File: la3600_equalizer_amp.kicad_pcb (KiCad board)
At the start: 2 copper layers, 54 parts, among them J1 JACK_TRS_3PINS, J2 JACK_TRS_3PINS, J3 USB_B, U1 LA3600, U2 LA3600, U3 LM386, U4 LM386

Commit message: some more pcb layout work
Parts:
- moved C32 4.00 mm to (176.7, 66.9), turned to 90 degrees
- moved C33 3.65 mm to (176.5, 94.6), turned to 90 degrees
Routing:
- net Vcc: track 11.9 -> 205.0 mm, vias 0 -> 2
- net Net-(22K6-Pad4): track 0.00 -> 133.1 mm, vias 0 -> 2
- net Net-(22K1-Pad1): track 145.5 -> 226.1 mm, vias 8 -> 10
- net Net-(22K6-Pad1): track 0.00 -> 74.1 mm
- net Net-(22K1-Pad3): track 170.1 -> 236.0 mm, vias 0 -> 2
- net Net-(22K1-Pad4): track 161.6 -> 225.8 mm, vias 8 -> 10
- net Net-(C24-Pad1): track 0.00 -> 21.4 mm
- net Net-(C26-Pad1): track 0.00 -> 17.4 mm
- net Net-(C5-Pad1): track 0.00 -> 11.5 mm
- net Net-(C11-Pad2): track 0.00 -> 11.5 mm
- net Net-(C10-Pad2): track 0.00 -> 11.5 mm
- net Net-(C4-Pad1): track 0.00 -> 11.2 mm
- net Net-(C32-Pad1): track 0.00 -> 7.84 mm
- net Net-(C33-Pad1): track 0.00 -> 7.64 mm
- net Net-(C21-Pad1): track 0.00 -> 7.14 mm
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
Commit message: finish pcb layout
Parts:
- moved C35 8.92 mm to (202.2, 91.5), turned to 270 degrees
- moved C36 8.03 mm to (212.7, 68.6)
- moved C37 8.03 mm to (212.7, 80.6)
- moved J2 8.03 mm to (228.4, 74.4)
- moved C34 7.03 mm to (197.6, 63.5), turned to 270 degrees
- moved R4 3.18 mm to (198.1, 94.0), turned to 90 degrees
- moved R3 0.25 mm to (194.1, 66.0), turned to 90 degrees
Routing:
- net GND: track 0.00 -> 658.9 mm, vias 0 -> 12
- net Net-(22K6-Pad5): track 0.00 -> 71.8 mm, vias 0 -> 2
- net Net-(22K6-Pad2): track 0.00 -> 48.1 mm, vias 0 -> 2
- net Net-(C37-Pad1): track 0.00 -> 42.6 mm
- net Net-(C36-Pad2): track 0.00 -> 26.2 mm
- net Net-(C36-Pad1): track 0.00 -> 25.6 mm
- net Net-(C37-Pad2): track 0.00 -> 14.2 mm
- net Net-(J3-Pad5): track 0.00 -> 13.5 mm
- net Net-(C35-Pad1): track 0.00 -> 9.34 mm
- net Net-(C34-Pad1): track 0.00 -> 9.09 mm
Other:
- board outline added: 198.6 x 95 mm

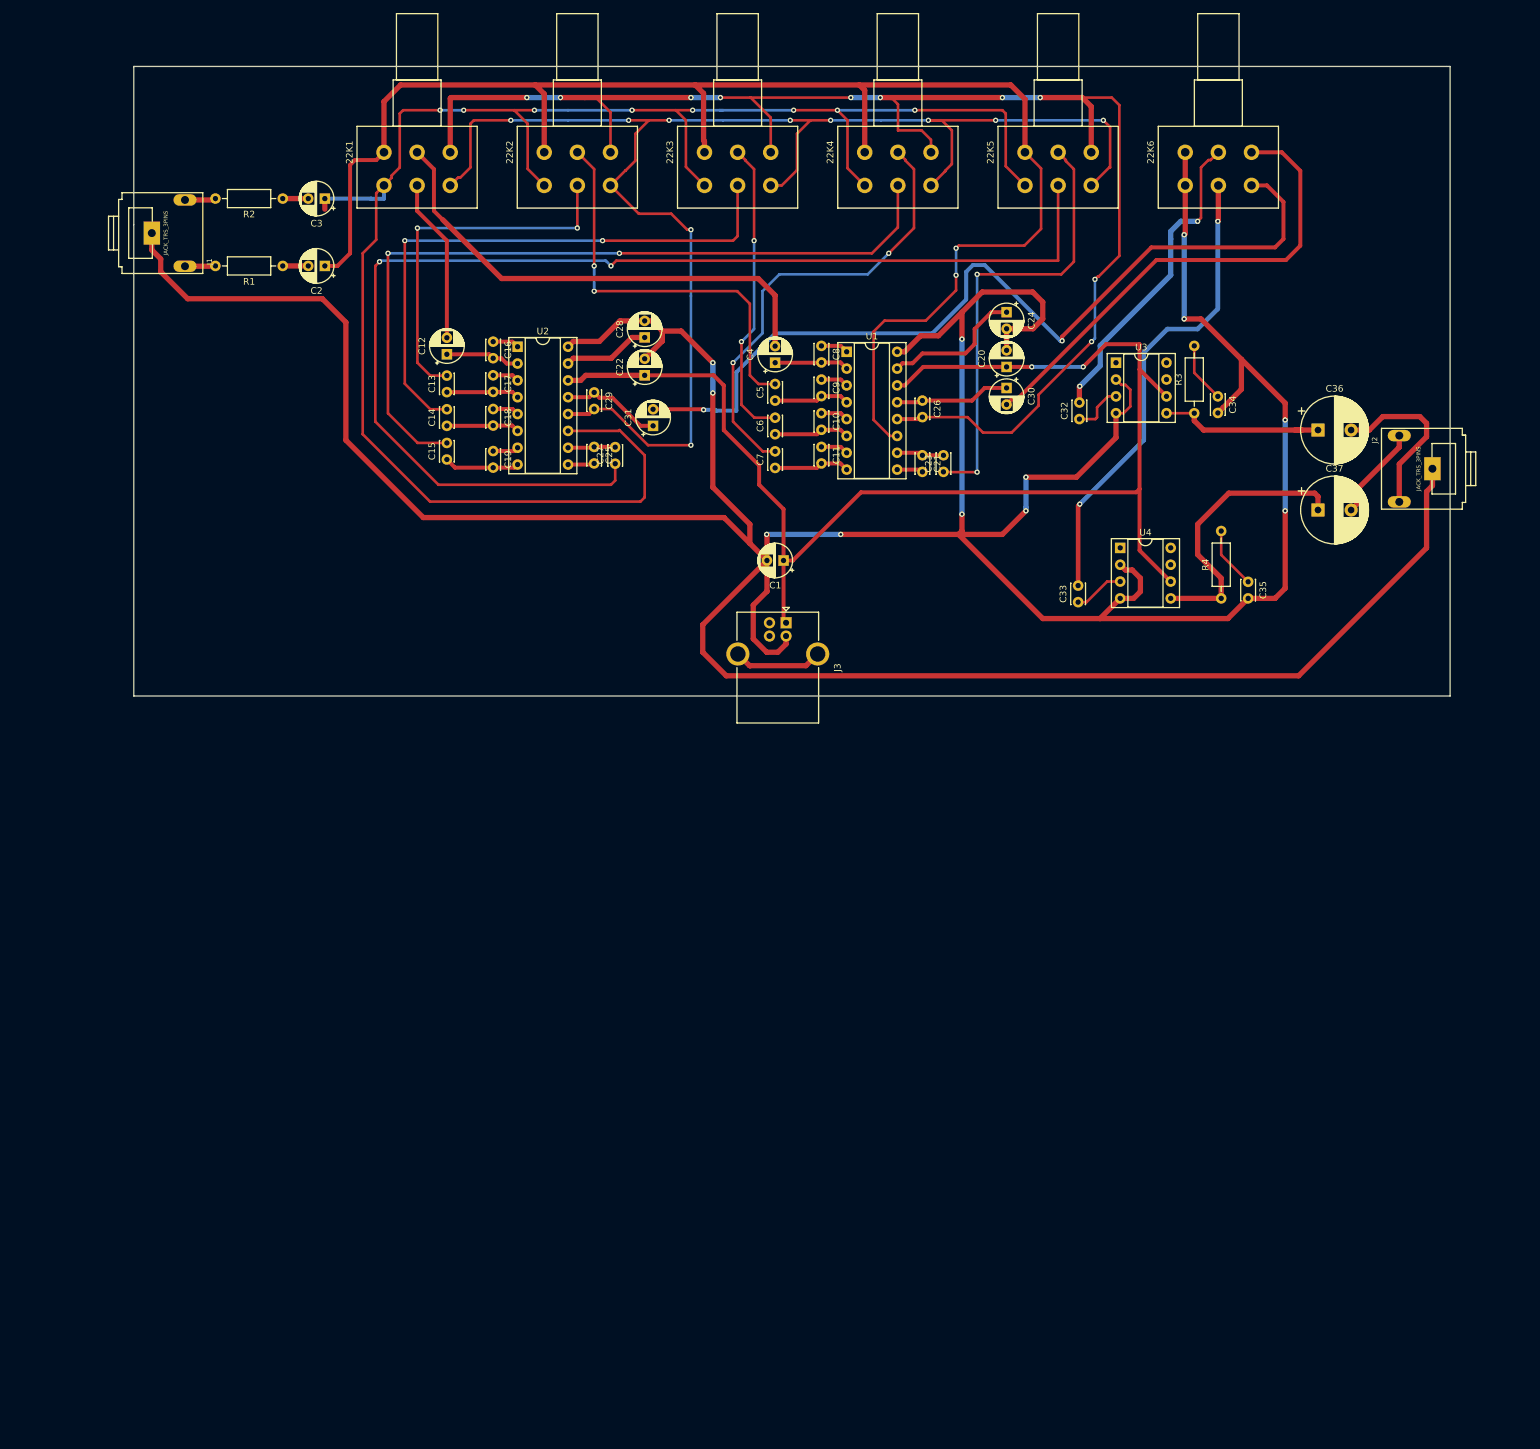
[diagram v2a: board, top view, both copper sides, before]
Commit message: rotate PCB + generate new gerber and excellon files
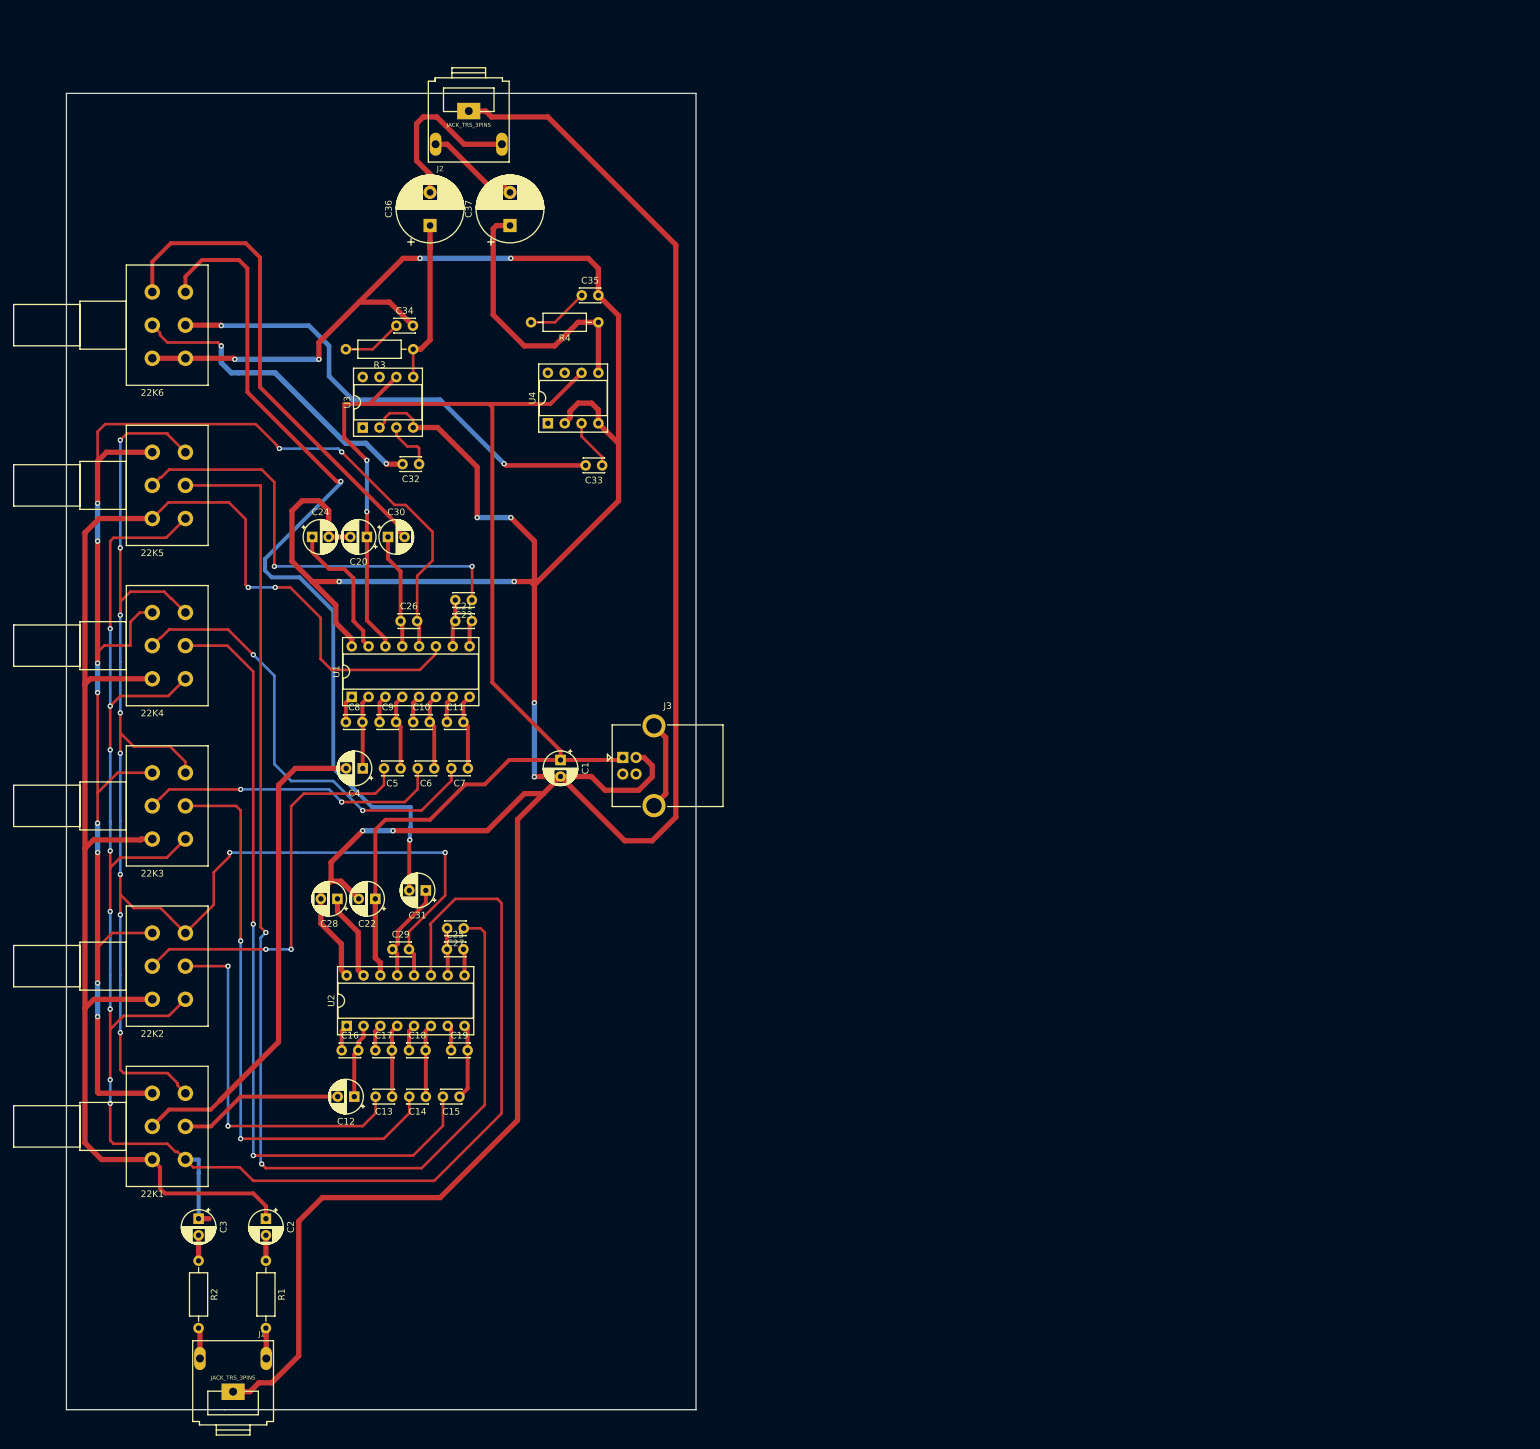
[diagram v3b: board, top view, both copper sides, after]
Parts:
- moved J1 173.6 mm to (49.0, 212.1), turned to 180 degrees
- moved 22K6 167.2 mm to (36.8, 47.8), turned to 180 degrees
- moved R2 160.8 mm to (43.8, 193.9), turned to 270 degrees
- moved C3 155.1 mm to (43.8, 187.6), turned to 270 degrees
- moved J2 153.1 mm to (84.6, 22.0), turned to 0 degrees
- moved R1 150.1 mm to (54.0, 193.9), turned to 270 degrees
- moved 22K1 148.9 mm to (36.8, 168.7), turned to 180 degrees
- moved 22K5 148.7 mm to (36.8, 71.9), turned to 180 degrees
- moved C2 144.0 mm to (54.0, 187.6), turned to 270 degrees
- moved C36 137.5 mm to (78.7, 37.7), turned to 90 degrees
- moved 22K2 136.6 mm to (36.8, 144.5), turned to 180 degrees
- moved 22K4 136.5 mm to (36.8, 96.1), turned to 180 degrees
- moved 22K3 132.2 mm to (36.8, 120.3), turned to 180 degrees
- moved C37 129.3 mm to (90.8, 37.7), turned to 90 degrees
- moved C34 124.4 mm to (73.7, 52.8), turned to 0 degrees
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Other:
- board size 198.6 x 95 mm -> 95 x 198.6 mm

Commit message: kicad 5 modifications
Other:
- board text added: "Yovan Naumovski 2018"
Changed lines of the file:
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@@
-(kicad_pcb (version 20171130) (host pcbnew 5.0.0-fee4fd1~65~ubuntu16.04.1)
+(kicad_pcb (version 20171130) (host pcbnew 5.0.0-fee4fd1~66~ubuntu16.04.1)
   (general
     (thickness 1.6)
-    (drawings 6)
+    (drawings 7)
     (tracks 633)
     (zones 0)
@@
     (descr "C, Disc series, Radial, pin pitch=2.50mm, , diameter*width=3*2mm^2, Capacitor")
     (tags "C Disc series Radial pin pitch 2.50mm  diameter 3mm width 2mm Capacitor")
-    (fp_text reference C21 (at 1.25 -2.25) (layer F.SilkS)
+    (fp_text reference C21 (at 4.826 0.127) (layer F.SilkS)
       (effects (font (size 1 1) (thickness 0.15)))
     )
@@
     (descr "C, Disc series, Radial, pin pitch=2.50mm, , diameter*width=3*2mm^2, Capacitor")
     (tags "C Disc series Radial pin pitch 2.50mm  diameter 3mm width 2mm Capacitor")
-    (fp_text reference C23 (at 1.25 -2.25 180) (layer F.SilkS)
+    (fp_text reference C23 (at -2.326 -0.254 180) (layer F.SilkS)
       (effects (font (size 1 1) (thickness 0.15)))
     )
@@
     )
   )
+  (gr_text "Yovan Naumovski 2018" (at 102.108 211.328) (layer F.SilkS)
+    (effects (font (size 1.5 1.5) (thickness 0.3)))
+  )
   (gr_line (start 47.752 216.408) (end 118.872 216.408) (layer Edge.Cuts) (width 0.15))
